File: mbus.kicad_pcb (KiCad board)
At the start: 2 copper layers, 32 parts, among them J1 USB_C_Receptacle_USB2.0, J2 MBUS, Q1 BC817, Q2 BC817, Q3 BC807, U1 AP3015, U2 USBLC6-2SC6, U3 CH340E

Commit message: PCB component placement WIP
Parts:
- moved R7 54.7 mm to (133.0, 73.3)
- moved R6 49.8 mm to (68.5, 80.8)
- moved R9 47.6 mm to (131.9, 87.7)
- moved R10 46.2 mm to (129.4, 85.5), turned to 180 degrees
- moved Q1 42.9 mm to (74.3, 81.8)
- moved R5 42.3 mm to (68.5, 82.5)
- moved R8 39.0 mm to (133.2, 76.7)
- moved J2 34.1 mm to (156.4, 87.7)
- moved L1 33.0 mm to (72.0, 73.7), turned to 0 degrees
- moved D1 32.1 mm to (77.1, 72.3), turned to -90 degrees
- moved D3 30.2 mm to (147.9, 85.2)
- moved U1 27.2 mm to (71.1, 68.4), turned to 180 degrees
- moved C1 25.6 mm to (67.7, 68.6), turned to 90 degrees
- moved D2 23.9 mm to (141.5, 85.2)
- moved R3 23.3 mm to (73.8, 65.2), turned to 180 degrees
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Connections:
- net Net-(F1-Pad1) renamed /USB_FUSE
- net Net-(J1-PadA5) renamed /USB_CC1
- net Net-(J1-PadB5) renamed /USB_CC2
- U2 pad 1: /USB_CONN_D- -> /USB_CONN_D+
- U2 pad 3: /USB_CONN_D+ -> /USB_CONN_D-
- U2 pad 4: /USB_D+ -> /USB_D-
- U2 pad 6: /USB_D- -> /USB_D+
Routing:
- net VBUS: track 0.00 -> 6.29 mm
- net GND: track 0.00 -> 1.16 mm, vias 0 -> 1

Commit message: PCB placement done
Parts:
- added G***: LOGO, LOGO, F.Cu at (98.2, 86.8)
- moved R8 60.3 mm to (73.1, 80.8), turned to 180 degrees
- moved R7 57.9 mm to (75.7, 81.5), turned to 90 degrees
- moved R10 56.7 mm to (73.1, 79.0)
- moved R11 56.2 mm to (80.7, 79.0)
- moved D2 56.2 mm to (85.8, 78.5)
- moved D3 56.2 mm to (92.1, 78.5)
- moved J2 56.2 mm to (100.7, 81.1)
- moved Q2 56.2 mm to (77.0, 77.9)
- moved R12 56.2 mm to (77.0, 74.8)
- moved Q3 56.1 mm to (80.7, 76.0)
- moved F2 55.9 mm to (80.8, 81.5)
- moved R9 55.0 mm to (77.3, 81.5), turned to 90 degrees
- moved C3 20.2 mm to (72.0, 87.8)
- moved R3 20.1 mm to (65.4, 83.5)
- moved R4 20.1 mm to (62.2, 83.5)
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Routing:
- net VBUS: track 6.29 -> 2.32 mm
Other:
- board text added: "+"
- board text added: "-"
- board text added: "Designed by Jan Gnip"
- board text added: "JLCJLCJLCJLC"
- board text added: "rev0.1"

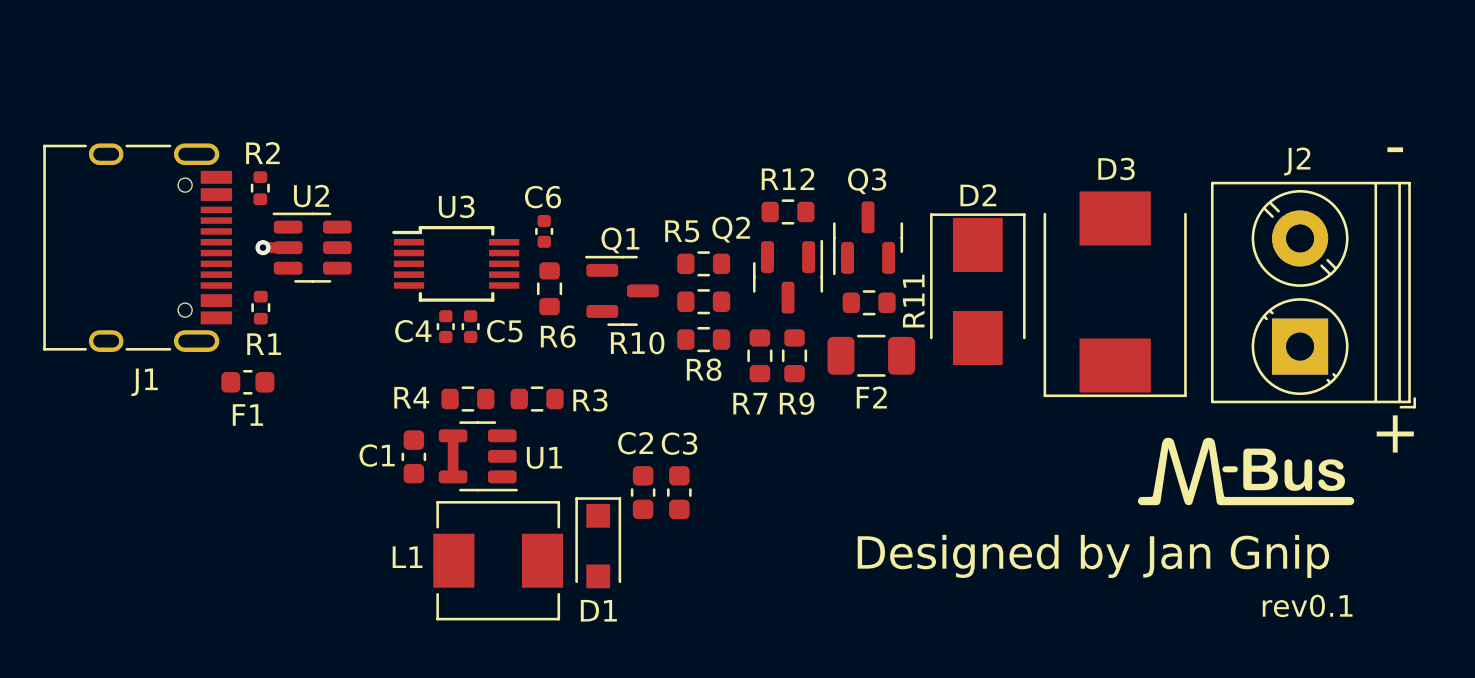
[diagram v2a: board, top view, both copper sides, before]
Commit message: Added mounting holes, board outline done
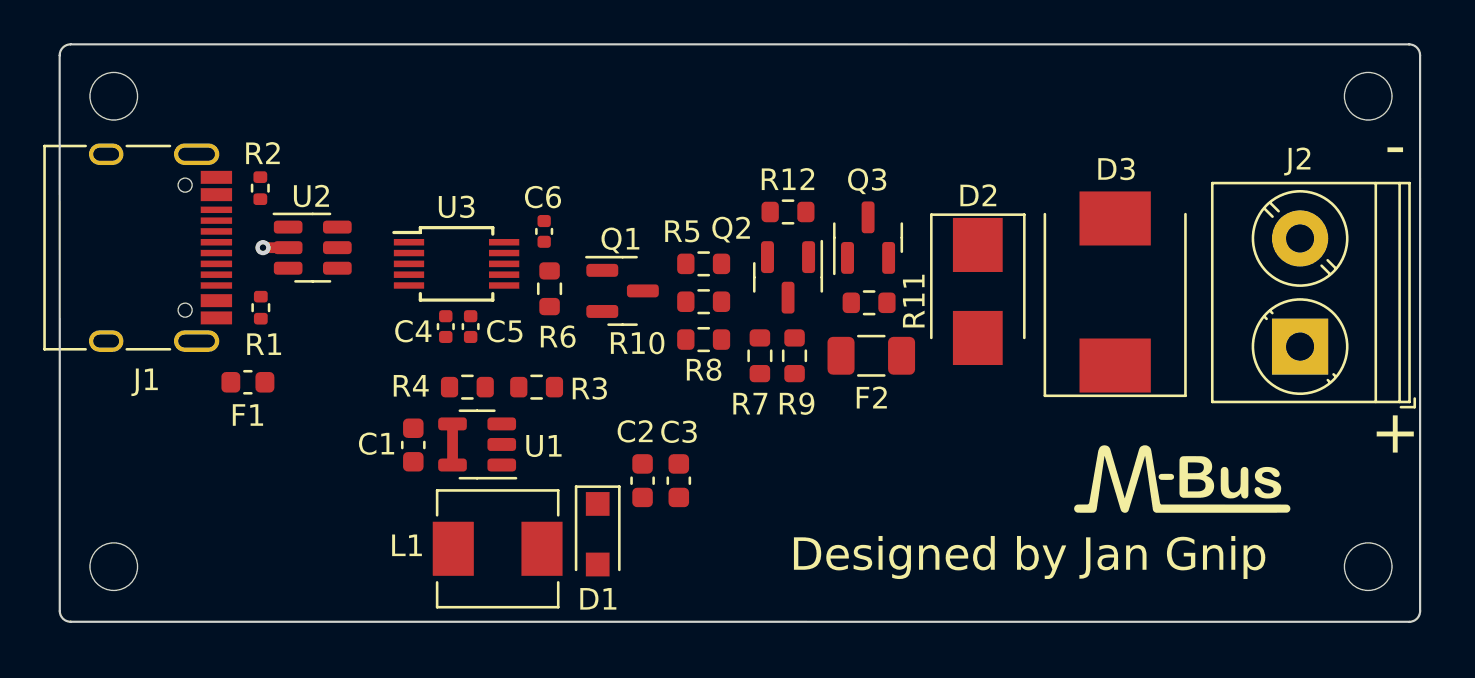
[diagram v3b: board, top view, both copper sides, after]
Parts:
- added H1: MountingHole, MountingHole:MountingHole_2.2mm_M2, F.Cu at (45.8, 91.2)
- added H2: MountingHole, MountingHole:MountingHole_2.2mm_M2, F.Cu at (103.8, 69.5)
- added H3: MountingHole, MountingHole:MountingHole_2.2mm_M2, F.Cu at (103.8, 91.2)
- added H4: MountingHole, MountingHole:MountingHole_2.2mm_M2, F.Cu at (45.8, 69.5)
- moved G*** 2.97 mm to (95.2, 87.2)
- moved U1 0.55 mm to (62.6, 85.6)
- moved C2 0.55 mm to (70.2, 87.3)
- moved C3 0.55 mm to (71.9, 87.3)
- moved D1 0.55 mm to (68.2, 89.8)
- moved L1 0.55 mm to (63.5, 90.4)
- moved R3 0.55 mm to (65.3, 83.0)
- moved C1 0.55 mm to (59.6, 85.6)
- moved R4 0.55 mm to (62.1, 83.0)
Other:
- board outline added: 62.9 x 26.7 mm
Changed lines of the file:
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@@
   (net 26 "unconnected-(U3-Pad6)")
   (net 27 "/USB_CC1")
+  (footprint "MountingHole:MountingHole_2.2mm_M2" (layer "F.Cu")
+    (at 45.8 69.5)
+    (descr "Mounting Hole 2.2mm, no annular, M2")
+    (tags "mounting hole 2.2mm no annular m2")
+    (property "Sheetfile" "mbus.kicad_sch")
+    (property "Sheetname" "")
+    (attr exclude_from_pos_files)
+    (fp_text reference "H4" (at 0 -3.2) (layer "F.Fab")
+      (effects (font (size 1 1) (thickness 0.15)))
+    )
+    (fp_text value "MountingHole" (at 0 3.2) (layer "F.Fab")
+      (effects (font (size 1 1) (thickness 0.15)))
+    )
+    (fp_text user "${REFERENCE}" (at 0 0) (layer "F.Fab")
+      (effects (font (size 1 1) (thickness 0.15)))
+    )
+    (fp_circle (center 0 0) (end 2.2 0) (layer "Cmts.User") (width 0.15) (fill none))
+    (fp_circle (center 0 0) (end 2.45 0) (layer "F.CrtYd") (width 0.05) (fill none))
+    (pad "" np_thru_hole circle (at 0 0) (size 2.2 2.2) (drill 2.2) (layers *.Cu *.Mask))
+  )
   (footprint "Package_TO_SOT_SMD:SOT-23" (layer "F.Cu")
     (at 80.675 76.0375 90)
@@
   )
   (footprint "Package_TO_SOT_SMD:SOT-23-5" (layer "F.Cu")
-    (at 62.625 86.15 180)
+    (at 62.6 85.6 180)
     (descr "SOT, 5 Pin (https://www.jedec.org/sites/default/files/docs/Mo-178c.PDF variant AA), generated with kicad-footprint-generator ipc_gullwing_generator.py")
     (tags "SOT TO_SOT_SMD")
@@
   )
   (footprint "Inductor_SMD:L_Sunlord_MWSA0518_5.4x5.2mm" (layer "F.Cu")
-    (at 63.575 90.975)
+    (at 63.55 90.425)
     (descr "Inductor, Sunlord, MWSA0518, 5.4mmx5.2mm")
     (tags "inductor Sunlord smd")
@@
     )
   )
+  (footprint "MountingHole:MountingHole_2.2mm_M2" (layer "F.Cu")
+    (at 45.8 91.25)
+    (descr "Mounting Hole 2.2mm, no annular, M2")
+    (tags "mounting hole 2.2mm no annular m2")
+    (property "Sheetfile" "mbus.kicad_sch")
+    (property "Sheetname" "")
+    (attr exclude_from_pos_files)
+    (fp_text reference "H1" (at 0 -3.2) (layer "F.Fab")
+      (effects (font (size 1 1) (thickness 0.15)))
+    )
+    (fp_text value "MountingHole" (at 0 3.2) (layer "F.Fab")
+      (effects (font (size 1 1) (thickness 0.15)))
+    )
+    (fp_text user "${REFERENCE}" (at 0 0) (layer "F.Fab")
+      (effects (font (size 1 1) (thickness 0.15)))
+    )
+    (fp_circle (center 0 0) (end 2.2 0) (layer "Cmts.User") (width 0.15) (fill none))
+    (fp_circle (center 0 0) (end 2.45 0) (layer "F.CrtYd") (width 0.05) (fill none))
+    (pad "" np_thru_hole circle (at 0 0) (size 2.2 2.2) (drill 2.2) (layers *.Cu *.Mask))
+  )
   (footprint "Fuse:Fuse_1206_3216Metric" (layer "F.Cu")
     (at 80.825 81.5)
@@
   )
   (footprint "Capacitor_SMD:C_0603_1608Metric" (layer "F.Cu")
-    (at 70.275 87.825 90)
+    (at 70.25 87.275 90)
     (descr "Capacitor SMD 0603 (1608 Metric), square (rectangular) end terminal, IPC_7351 nominal, (Body size source: IPC-SM-782 page 76, https://www.pcb-3d.com/wordpress/wp-content/uploads/ipc-sm-782a_amendment_1_and_2.pdf), generated with kicad-footprint-generator")
     (tags "capacitor")
@@
   )
   (footprint "Diode_SMD:D_SOD-123F" (layer "F.Cu")
-    (at 68.2 90.3 -90)
+    (at 68.175 89.75 -90)
     (descr "D_SOD-123F")
     (tags "D_SOD-123F")
@@
   )
   (footprint "Resistor_SMD:R_0603_1608Metric" (layer "F.Cu")
-    (at 62.175 83.5 180)
+    (at 62.15 82.95 180)
     (descr "Resistor SMD 0603 (1608 Metric), square (rectangular) end terminal, IPC_7351 nominal, (Body size source: IPC-SM-782 page 72, https://www.pcb-3d.com/wordpress/wp-content/uploads/ipc-sm-782a_amendment_1_and_2.pdf), generated with kicad-footprint-generator")
     (tags "resistor")
@@
   )
   (footprint "Capacitor_SMD:C_0603_1608Metric" (layer "F.Cu")
-    (at 71.95 87.825 90)
+    (at 71.925 87.275 90)
     (descr "Capacitor SMD 0603 (1608 Metric), square (rectangular) end terminal, IPC_7351 nominal, (Body size source: IPC-SM-782 page 76, https://www.pcb-3d.com/wordpress/wp-content/uploads/ipc-sm-782a_amendment_1_and_2.pdf), generated with kicad-footprint-generator")
     (tags "capacitor")
@@
     )
   )
+  (footprint "MountingHole:MountingHole_2.2mm_M2" (layer "F.Cu")
+    (at 103.8 69.5)
+    (descr "Mounting Hole 2.2mm, no annular, M2")
+    (tags "mounting hole 2.2mm no annular m2")
+    (property "Sheetfile" "mbus.kicad_sch")
+    (property "Sheetname" "")
+    (attr exclude_from_pos_files)
+    (fp_text reference "H2" (at 0 -3.2) (layer "F.Fab")
+      (effects (font (size 1 1) (thickness 0.15)))
+    )
+    (fp_text value "MountingHole" (at 0 3.2) (layer "F.Fab")
+      (effects (font (size 1 1) (thickness 0.15)))
+    )
+    (fp_text user "${REFERENCE}" (at 0 0) (layer "F.Fab")
+      (effects (font (size 1 1) (thickness 0.15)))
+    )
+    (fp_circle (center 0 0) (end 2.2 0) (layer "Cmts.User") (width 0.15) (fill none))
+    (fp_circle (center 0 0) (end 2.45 0) (layer "F.CrtYd") (width 0.05) (fill none))
+    (pad "" np_thru_hole circle (at 0 0) (size 2.2 2.2) (drill 2.2) (layers *.Cu *.Mask))
+  )
   (footprint "Package_TO_SOT_SMD:SOT-23" (layer "F.Cu")
     (at 69.325 78.5)
@@
   )
   (footprint "LOGO" (layer "F.Cu")
-    (at 98.15 86.85)
+    (at 95.2 87.2)
     (attr board_only exclude_from_pos_files exclude_from_bom)
     (fp_text reference "G***" (at 0 0) (layer "F.SilkS") hide
@@
   )
   (footprint "Resistor_SMD:R_0603_1608Metric" (layer "F.Cu")
-    (at 65.375 83.5 180)
+    (at 65.35 82.95 180)
     (descr "Resistor SMD 0603 (1608 Metric), square (rectangular) end terminal, IPC_7351 nominal, (Body size source: IPC-SM-782 page 72, https://www.pcb-3d.com/wordpress/wp-content/uploads/ipc-sm-782a_amendment_1_and_2.pdf), generated with kicad-footprint-generator")
     (tags "resistor")
@@
     )
   )
+  (footprint "MountingHole:MountingHole_2.2mm_M2" (layer "F.Cu")
+    (at 103.8 91.25)
+    (descr "Mounting Hole 2.2mm, no annular, M2")
+    (tags "mounting hole 2.2mm no annular m2")
+    (property "Sheetfile" "mbus.kicad_sch")
+    (property "Sheetname" "")
+    (attr exclude_from_pos_files)
+    (fp_text reference "H3" (at 0 -3.2) (layer "F.Fab")
+      (effects (font (size 1 1) (thickness 0.15)))
+    )
+    (fp_text value "MountingHole" (at 0 3.2) (layer "F.Fab")
+      (effects (font (size 1 1) (thickness 0.15)))
+    )
+    (fp_text user "${REFERENCE}" (at 0 0) (layer "F.Fab")
+      (effects (font (size 1 1) (thickness 0.15)))
+    )
+    (fp_circle (center 0 0) (end 2.2 0) (layer "Cmts.User") (width 0.15) (fill none))
+    (fp_circle (center 0 0) (end 2.45 0) (layer "F.CrtYd") (width 0.05) (fill none))
+    (pad "" np_thru_hole circle (at 0 0) (size 2.2 2.2) (drill 2.2) (layers *.Cu *.Mask))
+  )
   (footprint "Resistor_SMD:R_0402_1005Metric" (layer "F.Cu")
     (at 52.575 73.75 -90)
@@
   )
   (footprint "Capacitor_SMD:C_0603_1608Metric" (layer "F.Cu")
-    (at 59.675 86.175 90)
+    (at 59.65 85.625 90)
     (descr "Capacitor SMD 0603 (1608 Metric), square (rectangular) end terminal, IPC_7351 nominal, (Body size source: IPC-SM-782 page 76, https://www.pcb-3d.com/wordpress/wp-content/uploads/ipc-sm-782a_amendment_1_and_2.pdf), generated with kicad-footprint-generator")
     (tags "capacitor")
@@
     )
   )
+  (gr_arc (start 105.694976 67.101471) (mid 106.05 67.25) (end 106.198529 67.605024) (layer "Edge.Cuts") (width 0.1))
+  (gr_line (start 105.7 93.8) (end 43.803553 93.796447) (layer "Edge.Cuts") (width 0.1))
+  (gr_line (start 106.198529 67.605024) (end 106.2 93.3) (layer "Edge.Cuts") (width 0.1))
+  (gr_arc (start 43.803553 93.796447) (mid 43.45 93.65) (end 43.303553 93.296447) (layer "Edge.Cuts") (width 0.1))
+  (gr_line (start 43.803553 67.1) (end 105.694976 67.101471) (layer "Edge.Cuts") (width 0.1))
+  (gr_line (start 43.303553 93.296447) (end 43.3 67.603553) (layer "Edge.Cuts") (width 0.1))
+  (gr_arc (start 43.3 67.603553) (mid 43.448529 67.248529) (end 43.803553 67.1) (layer "Edge.Cuts") (width 0.1))
+  (gr_arc (start 106.2 93.3) (mid 106.053553 93.653553) (end 105.7 93.8) (layer "Edge.Cuts") (width 0.1))
+  (gr_text "rev0.1" (at 97.5 78.55 90) (layer "B.SilkS")
+    (effects (font (size 1 1) (thickness 0.15)) (justify mirror))
+  )
   (gr_text "JLCJLCJLCJLC" (at 104.1 78.65 90) (layer "B.SilkS")
     (effects (font (size 1 1) (thickness 0.153)) (justify mirror))
   )
-  (gr_text "rev0.1" (at 101 93.1) (layer "F.SilkS")
-    (effects (font (size 1 1) (thickness 0.15)))
-  )
   (gr_text "+" (at 105.05 85.05) (layer "F.SilkS")
     (effects (font (size 2 2) (thickness 0.5)))
@@
     (effects (font (size 2 2) (thickness 0.5)))
   )
-  (gr_text "Designed by Jan Gnip" (at 91.05 90.65) (layer "F.SilkS")
+  (gr_text "Designed by Jan Gnip" (at 88.1 90.7) (layer "F.SilkS")
     (effects (font (size 1.5 1.5) (thickness 0.3)))
   )
@@
   (via (at 52.7 76.5) (size 0.7) (drill 0.3) (layers "F.Cu" "B.Cu") (net 1))
   (segment (start 55.718573 76.5) (end 56.1375 76.5) (width 0.3) (layer "F.Cu") (net 8))
-  (segment (start 61.4875 87.1) (end 61.4875 85.2) (width 0.5) (layer "F.Cu") (net 8))
+  (segment (start 61.4625 86.55) (end 61.4625 84.65) (width 0.5) (layer "F.Cu") (net 8))
   (segment (start 50.545 76.25) (end 50.520489 76.274511) (width 0.2) (layer "F.Cu") (net 15))
 )

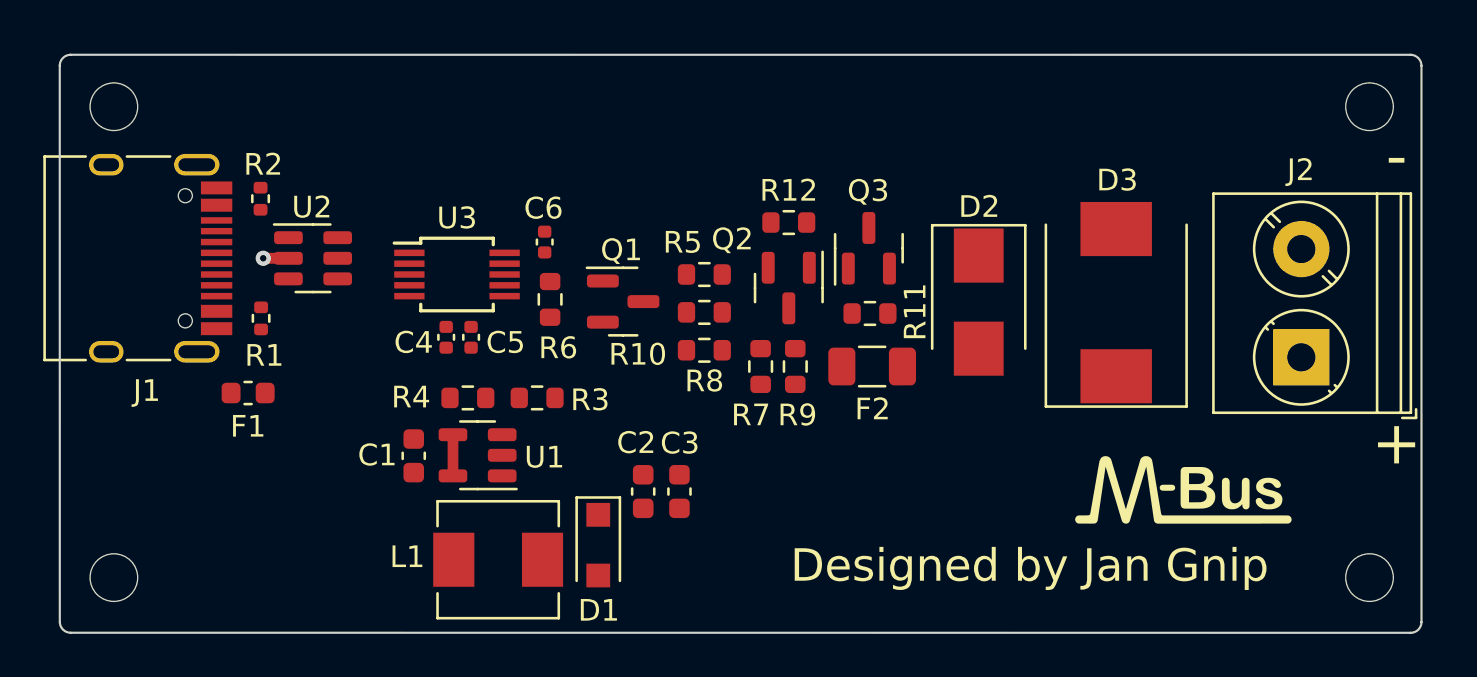
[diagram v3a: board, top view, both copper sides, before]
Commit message: PCB rev0.1 finished
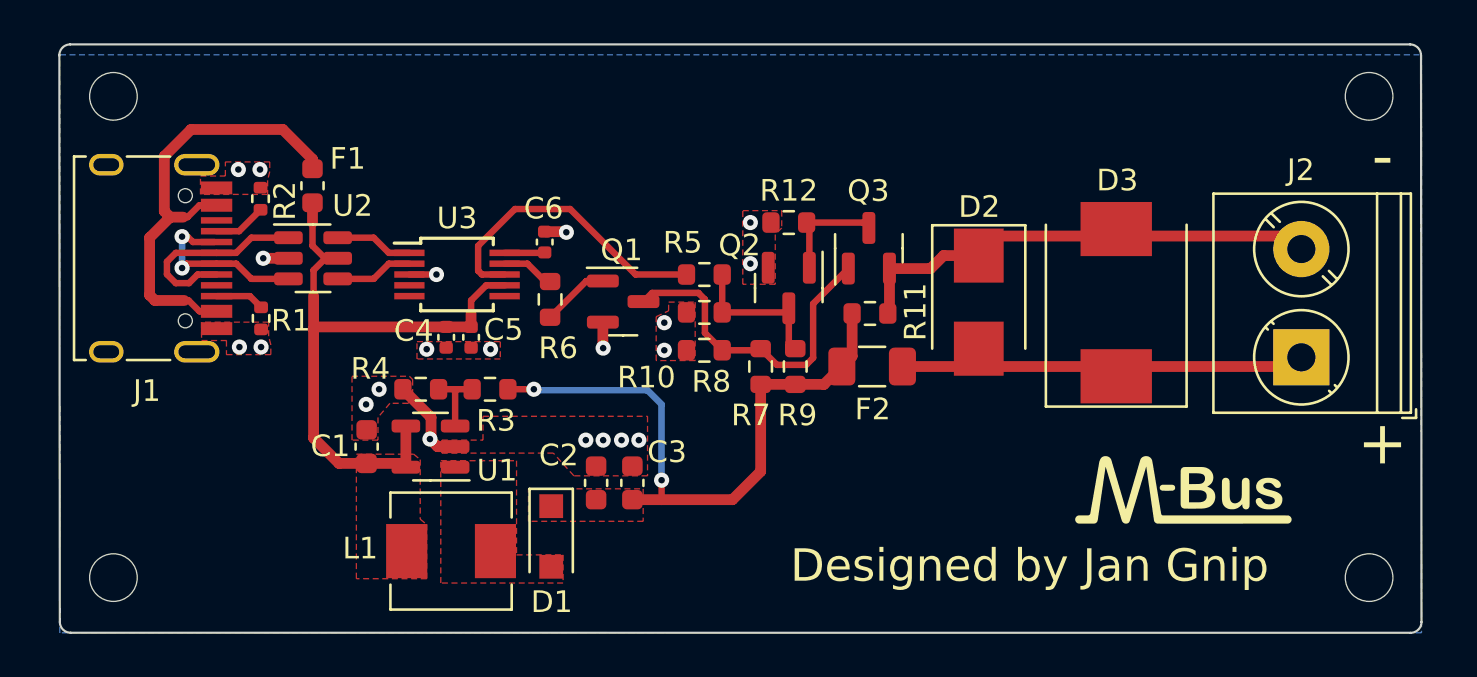
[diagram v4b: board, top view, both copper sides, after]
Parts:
- moved F1 10.0 mm to (55.0, 73.2), turned to -90 degrees
- moved C1 2.22 mm to (57.5, 85.2)
- moved U1 2.21 mm to (60.4, 85.2)
- moved C2 2.21 mm to (68.1, 86.9)
- moved C3 2.21 mm to (69.8, 86.9)
- moved D1 2.21 mm to (66.0, 89.3)
- moved R3 2.21 mm to (63.2, 82.5)
- moved R4 2.21 mm to (60.0, 82.5)
- moved L1 2.21 mm to (61.4, 90.0)
- moved H2 0.48 mm to (103.8, 69.0)
- moved H4 0.48 mm to (45.8, 69.0)
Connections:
- net Net-(D1-Pad2) renamed /BOOST_OUT
- net Net-(R3-Pad2) renamed /BOOST_FB
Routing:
- net +34V: track 0.00 -> 29.0 mm, vias 0 -> 2
- net VBUS: track 2.32 -> 29.6 mm
- net /-: track 0.00 -> 22.3 mm
- net /USB_FUSE: track 0.00 -> 21.1 mm
- net /+: track 0.00 -> 19.7 mm
- net Net-(Q1-Pad3): track 0.00 -> 15.3 mm
- net /UART_TX: track 0.00 -> 14.0 mm
- net /USB_CONN_D+: track 0.03 -> 9.28 mm
- net /USB_CONN_D-: track 0.00 -> 8.34 mm, vias 0 -> 2
- net GND: track 1.16 -> 8.80 mm, vias 1 -> 21
- net Net-(Q2-Pad3): track 0.00 -> 6.89 mm
- net Net-(Q2-Pad1): track 0.00 -> 5.12 mm
- net /USB_D-: track 0.00 -> 3.60 mm
- net /USB_D+: track 0.00 -> 3.60 mm
- net /BOOST_FB: track 0.00 -> 3.27 mm
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- added copper zone on F.Cu, net +34V
- added copper zone on F.Cu, net /BOOST_OUT
- added copper zone on B.Cu, net GND
- added copper zone on F.Cu, net GND
- added copper zone on F.Cu, net VBUS
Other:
- board size 62.9 x 26.7 mm -> 62.9 x 27.2 mm
- board text added: "4/22"
